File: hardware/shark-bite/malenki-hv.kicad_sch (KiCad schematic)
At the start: 21 parts, among them J1 Conn_01x02_Male-Connector, J2 Conn_01x08_Male, J3 Conn_01x02, U3 ATTiny1616-MNR

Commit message: Routed
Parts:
- D15: LCSC (none) -> C20883287
- U1: renamed from U2; value ~ -> GM7333; LCSC (none) -> C2833582
- renumbered C2 to C1, C3 to C2, C4 to C3, D1 to D2, D2 to D3, R7 to R1, R26 to R10, R8 to R2, R5 to R3, R6 to R4, R3 to R5, R4 to R6, R1 to R7, R2 to R8, R24 to R9, U3 to U2
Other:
- removed sheet motor_driver_2_left
- removed sheet motor_driver_3_right
- added sheet brushed_motor_driver (brushed_motor_driver.kicad_sch)
- added sheet brushed_motor_driver1 (brushed_motor_driver.kicad_sch)

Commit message: V0
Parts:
- removed C3: 100nF, Capacitor_SMD:C_0402_1005Metric_Pad0.74x0.62mm_HandSolder, symbol malenki-nano-rescue:C-Device
- removed D2: LED Blue, LED_SMD:LED_0603_1608Metric, symbol Device:LED
- removed D3: LED Red, LED_SMD:LED_0603_1608Metric, symbol Device:LED
- removed J2: Conn_01x08_Male, malenki-nano:SOIC_clipProgSmall, symbol Connector:Conn_01x08_Male
- removed J3: Conn_01x02, malenki-nano:wirepad_2, symbol Connector_Generic:Conn_01x02
- removed R1, R10, R2, R6: 10k, Resistor_SMD:R_0402_1005Metric, symbol malenki-nano-rescue:R-Device
- removed R3, R4, R7, R9: 470R, Resistor_SMD:R_0402_1005Metric, symbol malenki-nano-rescue:R-Device
- removed R5: 100k, Resistor_SMD:R_0402_1005Metric, symbol malenki-nano-rescue:R-Device
- removed R8: 1k, Resistor_SMD:R_0402_1005Metric, symbol malenki-nano-rescue:R-Device
- removed U2: ATTiny1616-MNR, Package_DFN_QFN:VQFN-20-1EP_3x3mm_P0.4mm_EP1.7x1.7mm, symbol MCU_Microchip_ATtiny:ATtiny1616-M
- added C10: 100nF, Capacitor_SMD:C_0603_1608Metric, symbol malenki-nano-rescue:C-Device
- added C11: 1uF, Capacitor_SMD:C_0603_1608Metric, symbol malenki-nano-rescue:C-Device
- added C6: 330uF, Capacitor_SMD:C_0603_1608Metric, symbol malenki-nano-rescue:C-Device
- added U3: LR645N8-G, TO-243AA_MCH, symbol Sharkbite:LR645N8-G
- renumbered D15 to D1
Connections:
- net GND: now also C10.2, C11.2, C6.2, U3.2 (GND)
- net VBAT renamed VBUS
- net VBUS: now also C11.1, C6.1, U3.1 (VIN)
- new net +10V: C10.1, U3.3 (VOUT)
- no-connect marks 6 -> 0
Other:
- removed sheet brushed_motor_driver
- removed sheet brushed_motor_driver1
- removed sheet radio
- sheet motor_driver_1_weapon ports: added none; removed MOTOR_PWM
- note removed: "BAD Regulator: HT7533-1 Better regulator: HT7333-1 OK regulator: Diodes AP2204RA-3.3TRG1"
- note removed: "MCU"
- note removed: "Programming / diagnostic"
- note removed: "Servo weapons (Weapon2 & Weapon3)"
- note removed: "Voltage sense"
- moved on the sheet: C1, C2, D1, J1, U1

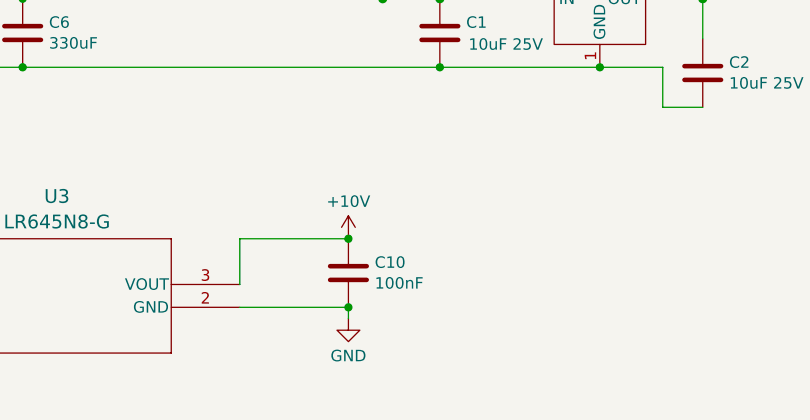
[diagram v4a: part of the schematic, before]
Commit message: Added tag-connect
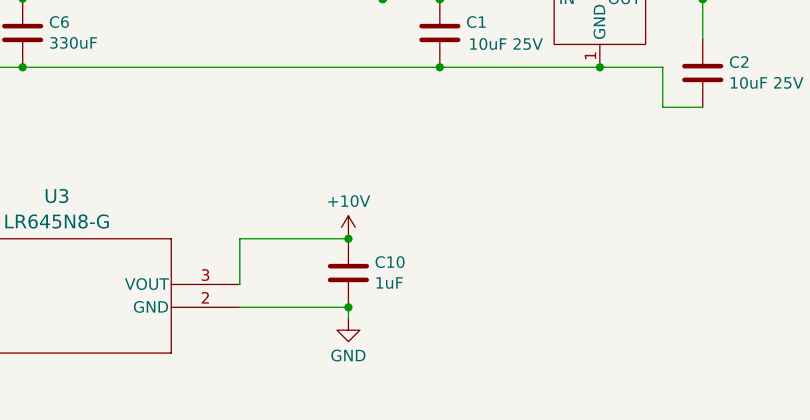
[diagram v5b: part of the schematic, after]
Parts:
- C10: value 100nF -> 1uF
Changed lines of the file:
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@@
 			)
 		)
-		(property "Value" "100nF"
+		(property "Value" "1uF"
 			(at 100.076 79.883 0)
 			(effects

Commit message: Update PCB
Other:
- note added: "Replace with https://www.lcsc.com/datasheet/lcsc_datasheet_2304140030_Diodes-Incorporated-AS78L15RTR-G1_C416201.pdf"
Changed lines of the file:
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@@
+		)
+	)
+	(text "Replace with https://www.lcsc.com/datasheet/lcsc_datasheet_2304140030_Diodes-Incorporated-AS78L15RTR-G1_C416201.pdf"
+		(exclude_from_sim no)
+		(at 83.82 104.902 0)
+		(effects
+			(font
+				(size 1.27 1.27)
+			)
 		)
 	)

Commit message: Minor Changes???
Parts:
- removed U3: LR645N8-G, TO-243AA_MCH, symbol Sharkbite:LR645N8-G
- added U3: ~, Package_TO_SOT_SMD:SOT-89-3, symbol Sharkbite:SOT-89-3_LDO
- C1, C2: value 10uF 25V -> 10uF; LCSC C96446 -> (none)
- C10, C11, C6: LCSC C96446 -> (none)
- J1: footprint malenki-nano:malenkipower -> Sharkbite:Power Input
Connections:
- net +10V: now also U3.3 (VOUT)
- net GND: now also U3.1 (VSS)
- net VBUS: now also U3.2 (VIN)
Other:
- moved on the sheet: C10

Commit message: Design Finished
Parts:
- C1: Vmax (none) -> 25V
- C2: Vmax (none) -> 5V
- U3: value ~ -> 78L10; LCSC (none) -> C6718417
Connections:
- net +10V: now also U3.1 (VOUT); no longer U3.3 (VOUT)
- net GND: now also U3.2 (VSS); no longer U3.1 (VSS)
- net VBUS: now also U3.3 (VIN); no longer U3.2 (VIN)
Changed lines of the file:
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@@
-					(unit 1)
-				)
-				(path "/f41619e3-8cf2-4511-8a51-762d4de43197/b339fba4-a8e4-4c66-ad9c-610bd968ae93"
-					(reference "J1")
 					(unit 1)
 				)
@@
 			)
 		)
-		(property "Value" "~"
+		(property "Value" "78L10"
 			(at 66.04 77.8899 0)
 			(effects
@@
 			)
 		)
-		(property "Datasheet" ""
+		(property "Datasheet" "https://www.lcsc.com/datasheet/lcsc_datasheet_2401301629_DOWO-78L10_C6718417.pdf"
 			(at 66.04 77.47 0)
 			(effects
@@
 		)
 		(property "Vmax" ""
+			(at 66.04 77.47 0)
+			(effects
+				(font
+					(size 1.27 1.27)
+				)
+				(hide yes)
+			)
+		)
+		(property "LCSC" "C6718417"
 			(at 66.04 77.47 0)
 			(effects
@@
 		(on_board yes)
 		(dnp no)
+		(fields_autoplaced yes)
 		(property "Reference" "C2"
-			(at 139.446 55.3466 0)
+			(at 139.7 53.9749 0)
 			(effects
 				(font
@@
 		)
 		(property "Value" "10uF"
-			(at 139.446 57.658 0)
+			(at 139.7 56.5149 0)
 			(effects
 				(font
@@
 			)
 		)
-		(property "Vmax" ""
-			(at 136.525 56.515 0)
-			(effects
-				(font
-					(size 1.27 1.27)
-				)
+		(property "Vmax" "5V"
+			(at 139.7 59.0549 0)
+			(effects
+				(font
+					(size 1.27 1.27)
+				)
+				(justify left)
 			)
 		)
@@
 		(on_board yes)
 		(dnp no)
+		(fields_autoplaced yes)
 		(property "Reference" "C1"
-			(at 110.236 50.9016 0)
+			(at 110.49 49.5299 0)
 			(effects
 				(font
@@
 		)
 		(property "Value" "10uF"
-			(at 110.49 53.34 0)
+			(at 110.49 52.0699 0)
 			(effects
 				(font
@@
 			)
 		)
-		(property "Vmax" ""
-			(at 107.315 52.07 0)
-			(effects
-				(font
-					(size 1.27 1.27)
-				)
-			)
-		)
+		(property "Vmax" "25V"
+			(at 110.49 54.6099 0)
+			(effects
+				(font
+					(size 1.27 1.27)
+				)
+				(justify left)
+			)
+		)
